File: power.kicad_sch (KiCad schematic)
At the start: 10 parts, among them J3 USB_C_Receptacle_USB2.0_16P, J5 Power Select, U10 LMR51430XFDDCR, U6 USBLC6-2P6, U9 AMS1117-3.3

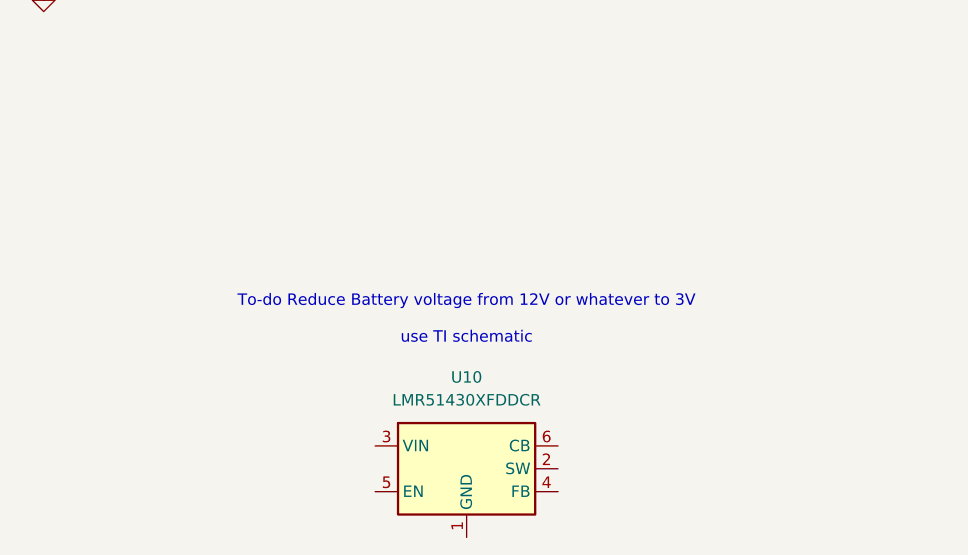
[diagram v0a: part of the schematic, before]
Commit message: added load capacitors to oscillator
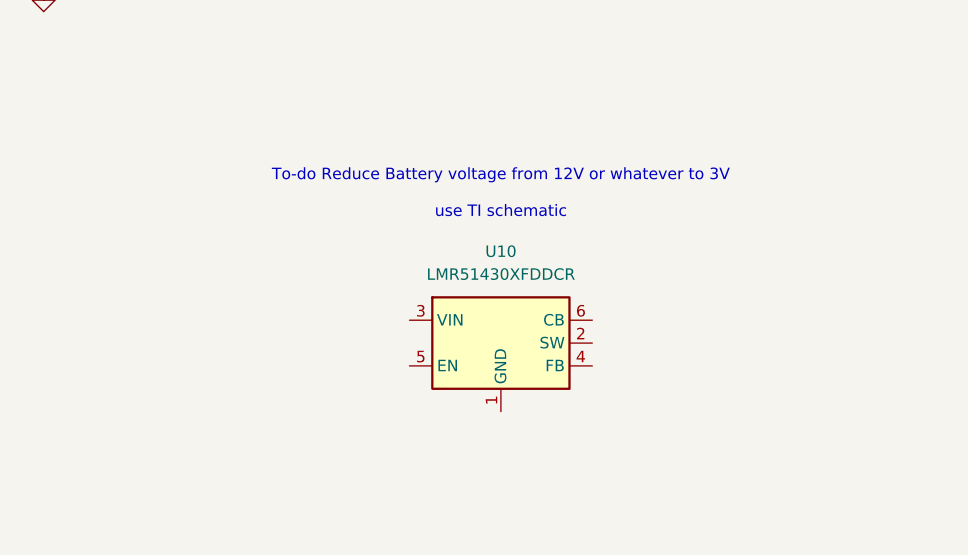
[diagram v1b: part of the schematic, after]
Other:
- moved on the sheet: U10
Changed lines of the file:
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@@
 	(text "To-do Reduce Battery voltage from 12V or whatever to 3V\n\nuse TI schematic"
 		(exclude_from_sim no)
-		(at 167.64 107.95 0)
+		(at 171.45 93.98 0)
 		(effects
 			(font
@@
 	(symbol
 		(lib_id "Regulator_Switching:LMR51430")
-		(at 167.64 124.46 0)
+		(at 171.45 110.49 0)
 		(unit 1)
 		(exclude_from_sim no)
@@
 		(fields_autoplaced yes)
 		(property "Reference" "U10"
-			(at 167.64 114.3 0)
+			(at 171.45 100.33 0)
 			(effects
 				(font
@@
 		)
 		(property "Value" "LMR51430XFDDCR"
-			(at 167.64 116.84 0)
+			(at 171.45 102.87 0)
 			(effects
 				(font
@@
 		)
 		(property "Footprint" "Package_TO_SOT_SMD:SOT-23-6"
-			(at 168.91 133.35 0)
+			(at 172.72 119.38 0)
 			(effects
 				(font
@@
 		)
 		(property "Datasheet" "https://www.ti.com/lit/ds/symlink/lmr51430.pdf"
-			(at 168.91 135.89 0)
+			(at 172.72 121.92 0)
 			(effects
 				(font
@@
 		)
 		(property "Description" "4.5-V to 36-V, 3-A synchronous buck converter with 40-µA IQ, SOT-23-6"
-			(at 167.64 124.46 0)
-			(effects
-				(font
+			(at 171.45 110.49 0)
+			(effects
+				(font

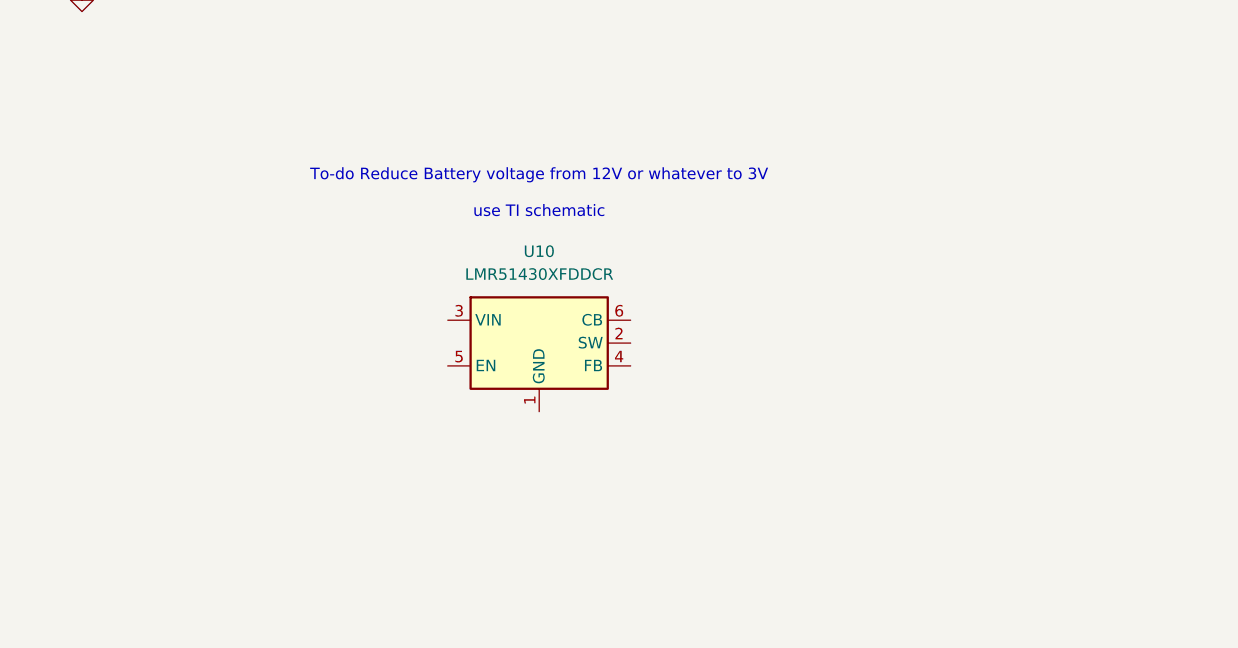
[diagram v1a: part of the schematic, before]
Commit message: Add voltage step down 12V to 3V3
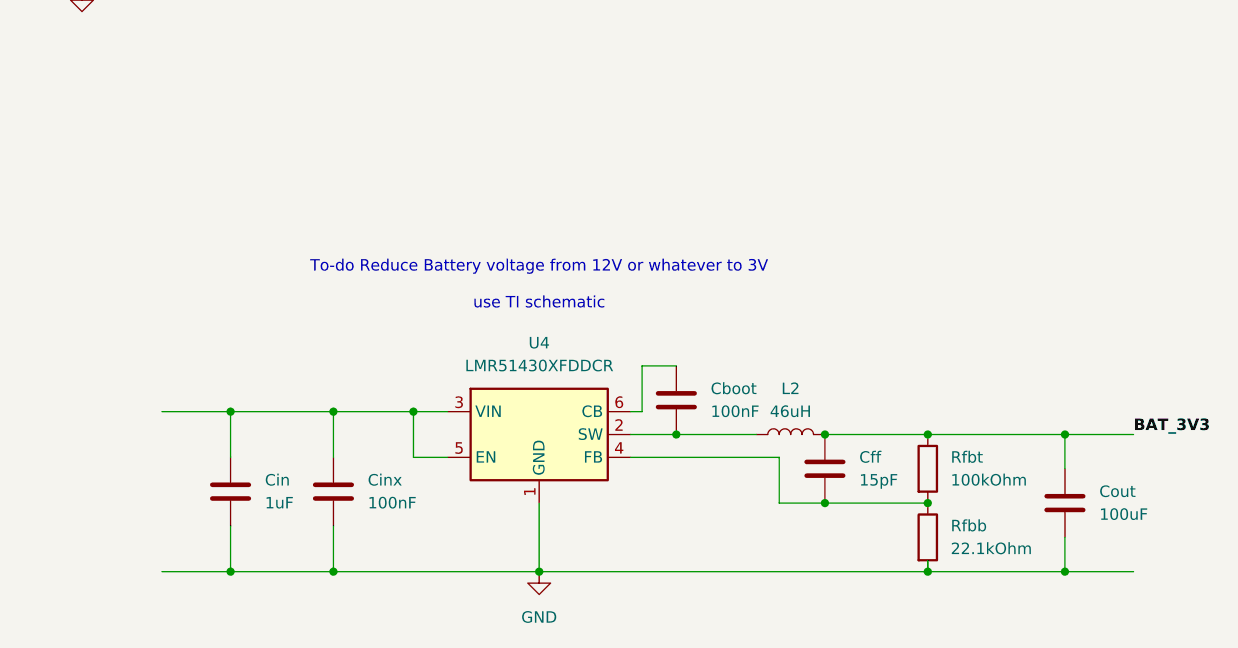
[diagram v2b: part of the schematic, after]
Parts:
- removed U10: LMR51430XFDDCR, Package_TO_SOT_SMD:SOT-23-6, symbol Regulator_Switching:LMR51430
- added Cboot, Cinx: 100nF, symbol Device:C
- added Cff: 15pF, symbol Device:C
- added Cin: 1uF, symbol Device:C
- added Cout: 100uF, symbol Device:C
- added L2: 46uH, symbol Device:L
- added Rfbb: 22.1kOhm, symbol Device:R
- added Rfbt: 100kOhm, symbol Device:R
- added U4: LMR51430XFDDCR, Package_TO_SOT_SMD:SOT-23-6, symbol Regulator_Switching:LMR51430
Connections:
- net BAT_3V3: now also Cff.1, Cout.1, L2.2, Rfbt.1
- net GND: now also Cin.2, Cinx.2, Cout.2, Rfbb.2, U4.1 (GND)
- new net: Cin.1, Cinx.1, U4.3 (VIN), U4.5 (EN)
- new net: Cff.2, Rfbb.1, Rfbt.2, U4.4 (FB)
- new net: Cboot.1, U4.6 (CB)
- new net: Cboot.2, L2.1, U4.2 (SW)

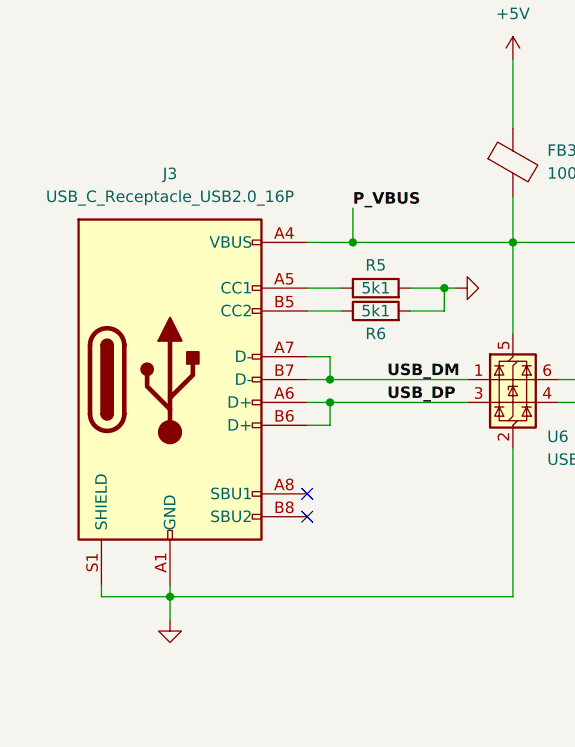
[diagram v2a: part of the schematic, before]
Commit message: Added voltage step down form 12V to 3V3
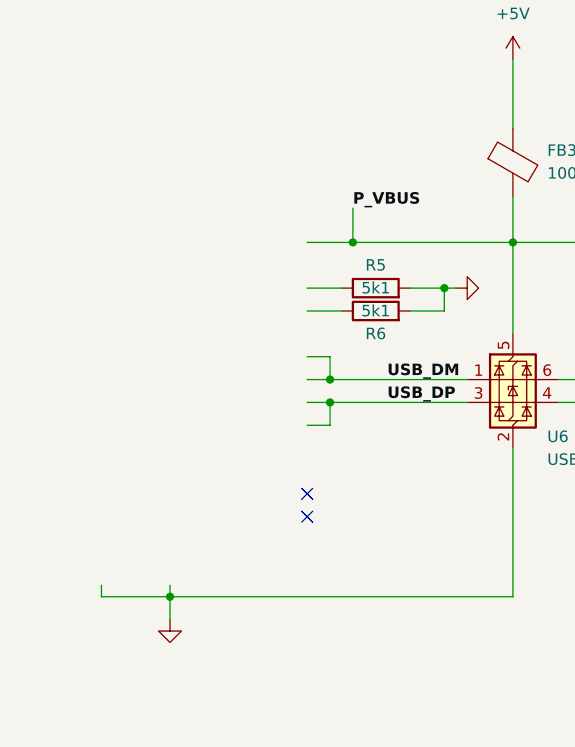
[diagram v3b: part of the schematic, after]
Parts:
- removed J3: USB_C_Receptacle_USB2.0_16P, symbol Connector:USB_C_Receptacle_USB2.0_16P
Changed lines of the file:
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@@
-	)
-	(symbol
-		(lib_id "Connector:USB_C_Receptacle_USB2.0_16P")
-		(at 39.37 73.66 0)
-		(unit 1)
-		(exclude_from_sim no)
-		(in_bom yes)
-		(on_board yes)
-		(dnp no)
-		(fields_autoplaced yes)
-		(property "Reference" "J3"
-			(at 39.37 50.8 0)
-			(effects
-				(font
-					(size 1.27 1.27)
-				)
-			)
-		)
-		(property "Value" "USB_C_Receptacle_USB2.0_16P"
-			(at 39.37 53.34 0)
-			(effects
-				(font
-					(size 1.27 1.27)
-				)
-			)
-		)
-		(property "Footprint" ""
-			(at 43.18 73.66 0)
-			(effects
-				(font
-					(size 1.27 1.27)
-				)
-				(hide yes)
-			)
-		)
-		(property "Datasheet" "https://www.usb.org/sites/default/files/documents/usb_type-c.zip"
-			(at 43.18 73.66 0)
-			(effects
-				(font
-					(size 1.27 1.27)
-				)
-				(hide yes)
-			)
-		)
-		(property "Description" "USB 2.0-only 16P Type-C Receptacle connector"
-			(at 39.37 73.66 0)
-			(effects
-				(font
-					(size 1.27 1.27)
-				)
-				(hide yes)
-			)
-		)
-		(pin "B8"
-		)
-		(pin "A7"
-		)
-		(pin "S1"
-		)
-		(pin "A1"
-		)
-		(pin "A8"
-		)
-		(pin "A5"
-		)
-		(pin "A12"
-		)
-		(pin "B1"
-		)
-		(pin "A4"
-		)
-		(pin "B12"
-		)
-		(pin "A6"
-		)
-		(pin "B6"
-		)
-		(pin "B7"
-		)
-		(pin "B5"
-		)
-		(pin "B9"
-		)
-		(pin "A9"
-		)
-		(pin "B4"
-		)
-		(instances
-			(project "nc_fc"
-				(path "/3f5bc5ea-feaa-4ed9-b0e0-c918b1fb5754/74cb3ba4-5441-4040-b144-f529fa281743"
-					(reference "J3")
-					(unit 1)
-				)
-			)
-		)
 	)
 	(symbol

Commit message: added usbc receptacle back
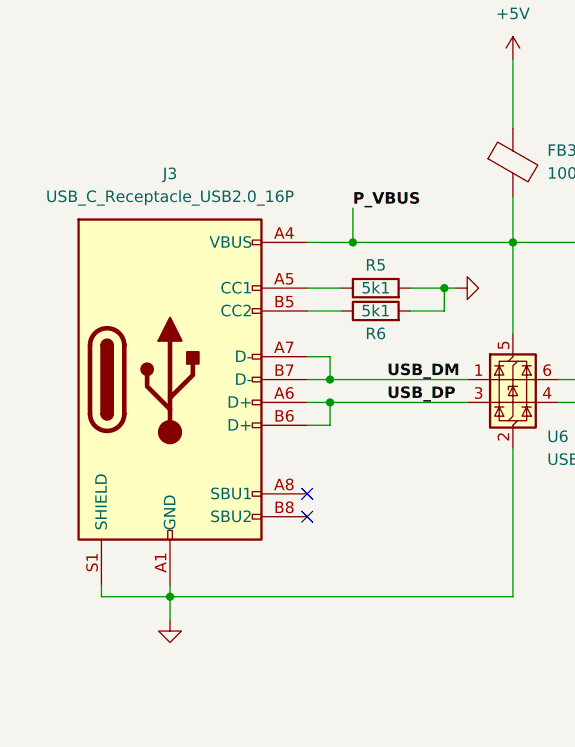
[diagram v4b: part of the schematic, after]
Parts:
- added J3: USB_C_Receptacle_USB2.0_16P, symbol Connector:USB_C_Receptacle_USB2.0_16P
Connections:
- net GND: now also J3.A1 (GND), J3.A12 (GND), J3.B1 (GND), J3.B12 (GND), J3.S1 (SHIELD)
- net P_VBUS: now also J3.A4 (VBUS), J3.A9 (VBUS), J3.B4 (VBUS), J3.B9 (VBUS)
- net USB_DM: now also J3.A7 (D-), J3.B7 (D-)
- net USB_DP: now also J3.A6 (D+), J3.B6 (D+)
- net at R5.1: now also J3.A5 (CC1)
- net at R6.1: now also J3.B5 (CC2)
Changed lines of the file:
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@@
+	)
+	(symbol
+		(lib_id "Connector:USB_C_Receptacle_USB2.0_16P")
+		(at 39.37 73.66 0)
+		(unit 1)
+		(exclude_from_sim no)
+		(in_bom yes)
+		(on_board yes)
+		(dnp no)
+		(fields_autoplaced yes)
+		(property "Reference" "J3"
+			(at 39.37 50.8 0)
+			(effects
+				(font
+					(size 1.27 1.27)
+				)
+			)
+		)
+		(property "Value" "USB_C_Receptacle_USB2.0_16P"
+			(at 39.37 53.34 0)
+			(effects
+				(font
+					(size 1.27 1.27)
+				)
+			)
+		)
+		(property "Footprint" ""
+			(at 43.18 73.66 0)
+			(effects
+				(font
+					(size 1.27 1.27)
+				)
+				(hide yes)
+			)
+		)
+		(property "Datasheet" "https://www.usb.org/sites/default/files/documents/usb_type-c.zip"
+			(at 43.18 73.66 0)
+			(effects
+				(font
+					(size 1.27 1.27)
+				)
+				(hide yes)
+			)
+		)
+		(property "Description" "USB 2.0-only 16P Type-C Receptacle connector"
+			(at 39.37 73.66 0)
+			(effects
+				(font
+					(size 1.27 1.27)
+				)
+				(hide yes)
+			)
+		)
+		(pin "B8"
+		)
+		(pin "A7"
+		)
+		(pin "S1"
+		)
+		(pin "A1"
+		)
+		(pin "A8"
+		)
+		(pin "A5"
+		)
+		(pin "A12"
+		)
+		(pin "B1"
+		)
+		(pin "A4"
+		)
+		(pin "B12"
+		)
+		(pin "A6"
+		)
+		(pin "B6"
+		)
+		(pin "B7"
+		)
+		(pin "B5"
+		)
+		(pin "B9"
+		)
+		(pin "A9"
+		)
+		(pin "B4"
+		)
+		(instances
+			(project "aerolotl"
+				(path "/3f5bc5ea-feaa-4ed9-b0e0-c918b1fb5754/74cb3ba4-5441-4040-b144-f529fa281743"
+					(reference "J3")
+					(unit 1)
+				)
+			)
+		)
 	)
 	(symbol
